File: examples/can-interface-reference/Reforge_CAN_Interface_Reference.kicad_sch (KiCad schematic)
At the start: 10 parts, among them J1 CAN / 12V INPUT, J2 REFORGE EXPANSION, U1 MCP1799T-3302H/TT, U2 SN65HVD230D

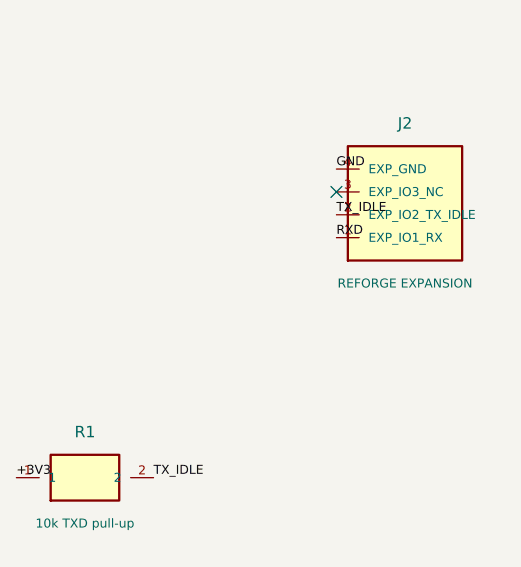
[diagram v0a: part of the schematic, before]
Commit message: Use Reforge JST GH connector on CAN reference
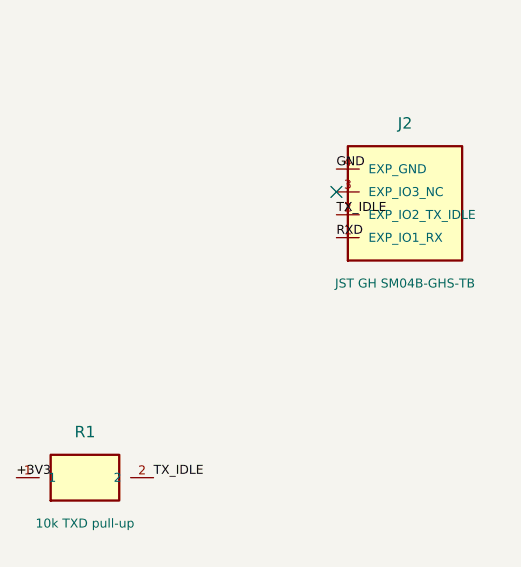
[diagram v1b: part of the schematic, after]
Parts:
- J2: value REFORGE EXPANSION -> JST GH SM04B-GHS-TB; footprint Connector_PinHeader_2.54mm:PinHeader_1x04_P2.54mm_Vertical -> Connector_JST:JST_GH_SM04B-GHS-TB_1x04-1MP_P1.25mm_Horizontal
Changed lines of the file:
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@@
       (exclude_from_sim no) (in_bom yes) (on_board yes) (dnp no)
       (property "Reference" "J2" (at 218.44 67.31 0) (effects (font (size 1.27 1.27))))
-      (property "Value" "REFORGE EXPANSION" (at 218.44 85.09 0) (effects (font (size 1.0 1.0))))
-      (property "Footprint" "Connector_PinHeader_2.54mm:PinHeader_1x04_P2.54mm_Vertical" (at 218.44 76.20 0) (hide yes) (effects (font (size 1.27 1.27))))
-      (property "Datasheet" "" (at 218.44 76.20 0) (hide yes) (effects (font (size 1.27 1.27))))
+      (property "Value" "JST GH SM04B-GHS-TB" (at 218.44 85.09 0) (effects (font (size 1.0 1.0))))
+      (property "Footprint" "Connector_JST:JST_GH_SM04B-GHS-TB_1x04-1MP_P1.25mm_Horizontal" (at 218.44 76.20 0) (hide yes) (effects (font (size 1.27 1.27))))
+      (property "Datasheet" "https://www.jst-mfg.com/product/pdf/eng/eGH.pdf" (at 218.44 76.20 0) (hide yes) (effects (font (size 1.27 1.27))))
       (property "Description" "Reforge CAN interface untested reference design" (at 218.44 76.20 0) (hide yes) (effects (font (size 1.27 1.27))))
       (pin "1") (pin "2") (pin "3") (pin "4")
